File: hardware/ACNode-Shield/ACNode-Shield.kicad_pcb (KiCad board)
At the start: 2 copper layers, 50 x 50 mm, 15 parts, among them J1 MICRO_SD_HINGE, P1 CONN_NFC, P2 CONN_RELAY, P3 CONN_RGB_LED, P4 CONN_X6, P5 CONN_X7, P6 CONN_WS2812, Q1 PN2222A, SW1 SW_RST, SW2 SW_BTN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

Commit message: Off to the fab.
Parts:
- moved P2 5.55 mm to (20.7, 15.3), turned to 90 degrees
- moved P3 0.61 mm to (52.8, 41.9)
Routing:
- net +5V: track 0.00 -> 129.1 mm
- net GND: track 0.00 -> 114.4 mm
- net +3.3v: track 0.00 -> 52.6 mm, vias 0 -> 1
- net PQ1: track 0.00 -> 41.1 mm
- net PQ3: track 0.00 -> 39.4 mm
- net PQ2: track 0.00 -> 34.5 mm
- net PQ0: track 0.00 -> 30.3 mm
- net Net-(D1-Pad2): track 0.00 -> 29.9 mm
- net Net-(P2-Pad2): track 0.00 -> 27.7 mm
- net Net-(P2-Pad3): track 0.00 -> 22.0 mm
- net PG1: track 0.00 -> 19.2 mm
- net PP5: track 0.00 -> 18.4 mm
- net /RESET: track 0.00 -> 18.2 mm
- net PM7: track 0.00 -> 17.1 mm
- net Net-(Q1-Pad2): track 0.00 -> 8.41 mm
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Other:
- net class Relay added: clearance 0.2, trace_width 0.5, via_dia 1.2, via_drill 1
- board text added: "LHS ACNode Shield rev 1"

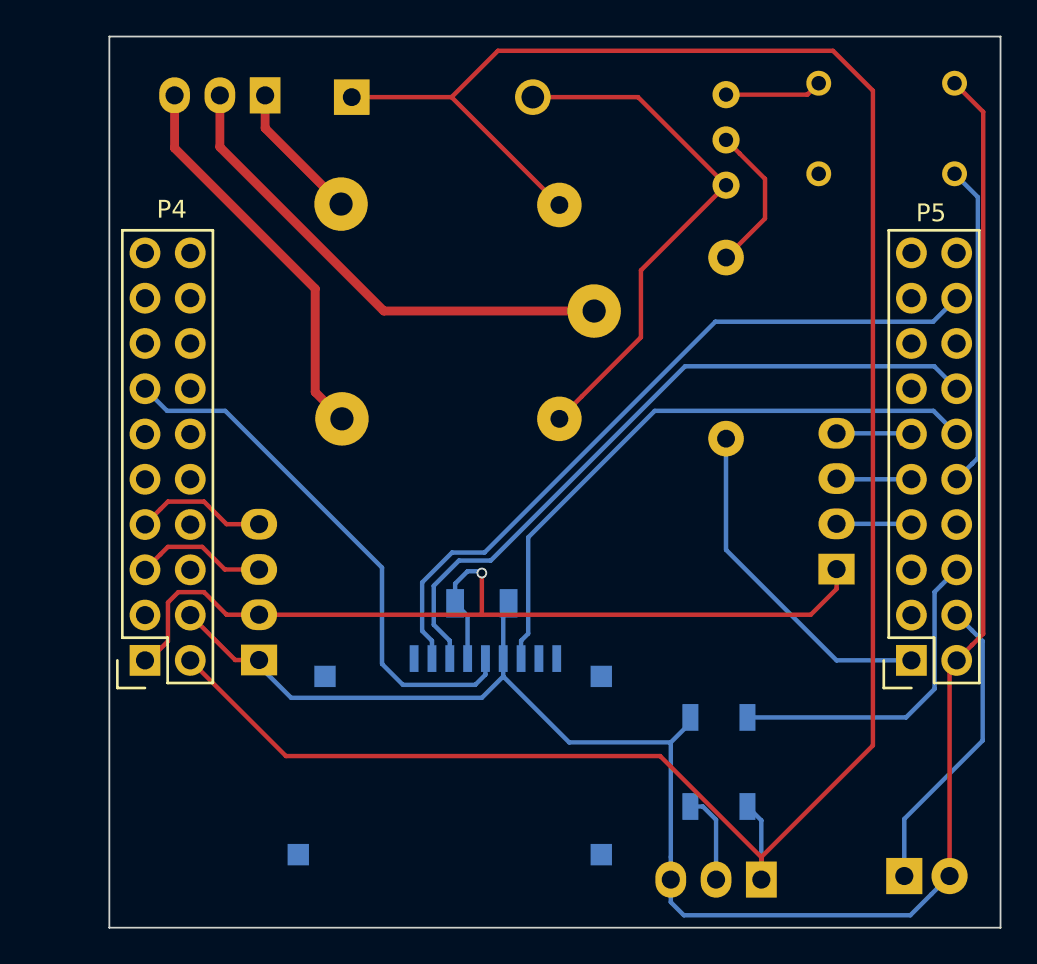
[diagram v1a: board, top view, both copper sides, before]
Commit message: Updated the MicroSD slot component, based on precise drawings.
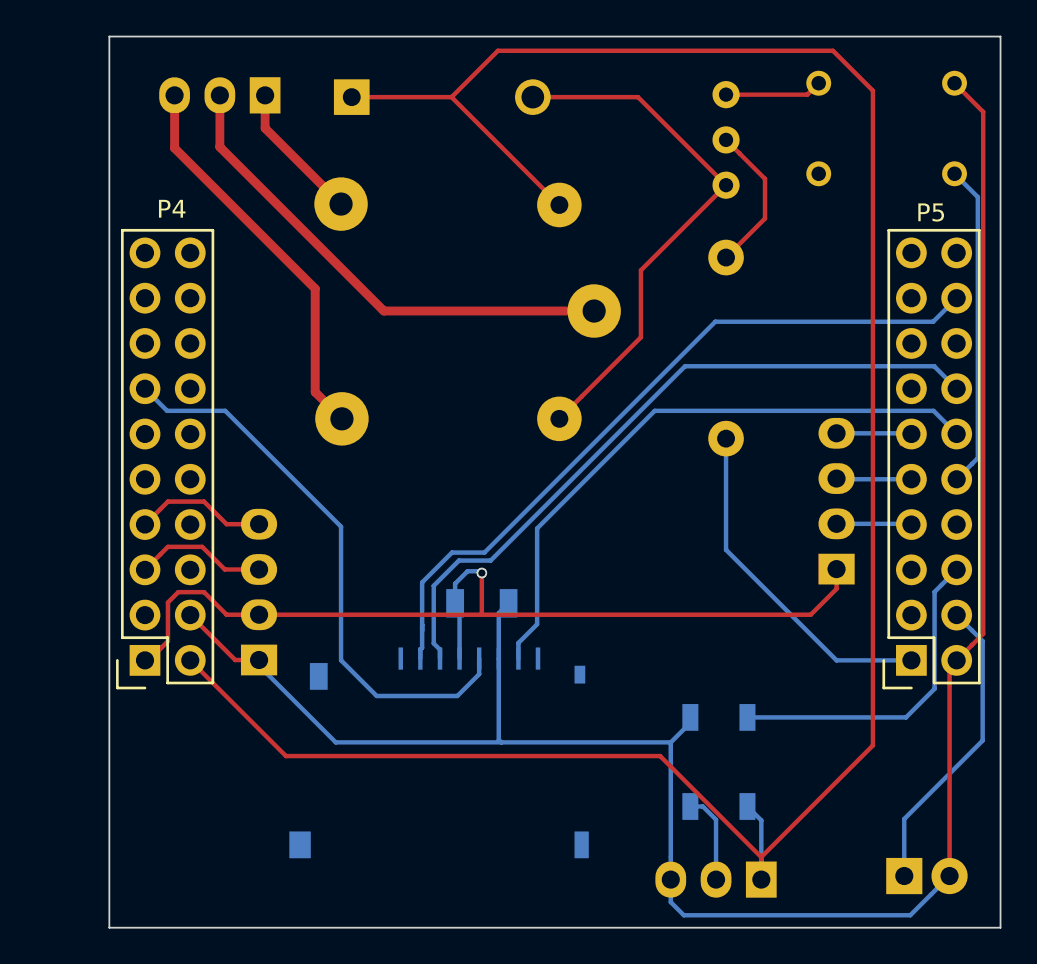
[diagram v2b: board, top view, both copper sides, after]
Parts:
- J1: footprint MicroSD:MICRO_SD_HINGE_CHINA -> SD_Slots:MicroSD_Slot
- moved J1 6.26 mm to (27.0, 54.0), turned to 180 degrees
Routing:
- net GND: track 114.4 -> 117.7 mm
- net PQ0: track 30.3 -> 31.7 mm
